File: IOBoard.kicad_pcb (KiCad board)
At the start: 2 copper layers, 99.4 x 47.1 mm, 49 parts, among them J1 Conn_02x05_Odd_Even, J10 Conn_01x03, J11 Conn_01x03, J2 Conn_02x05_Odd_Even, J3 Conn_02x05_Odd_Even, J4 Conn_02x05_Odd_Even, J5 Conn_02x05_Odd_Even, J6 Conn_01x03, J7 Conn_01x03, J8 Conn_01x03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

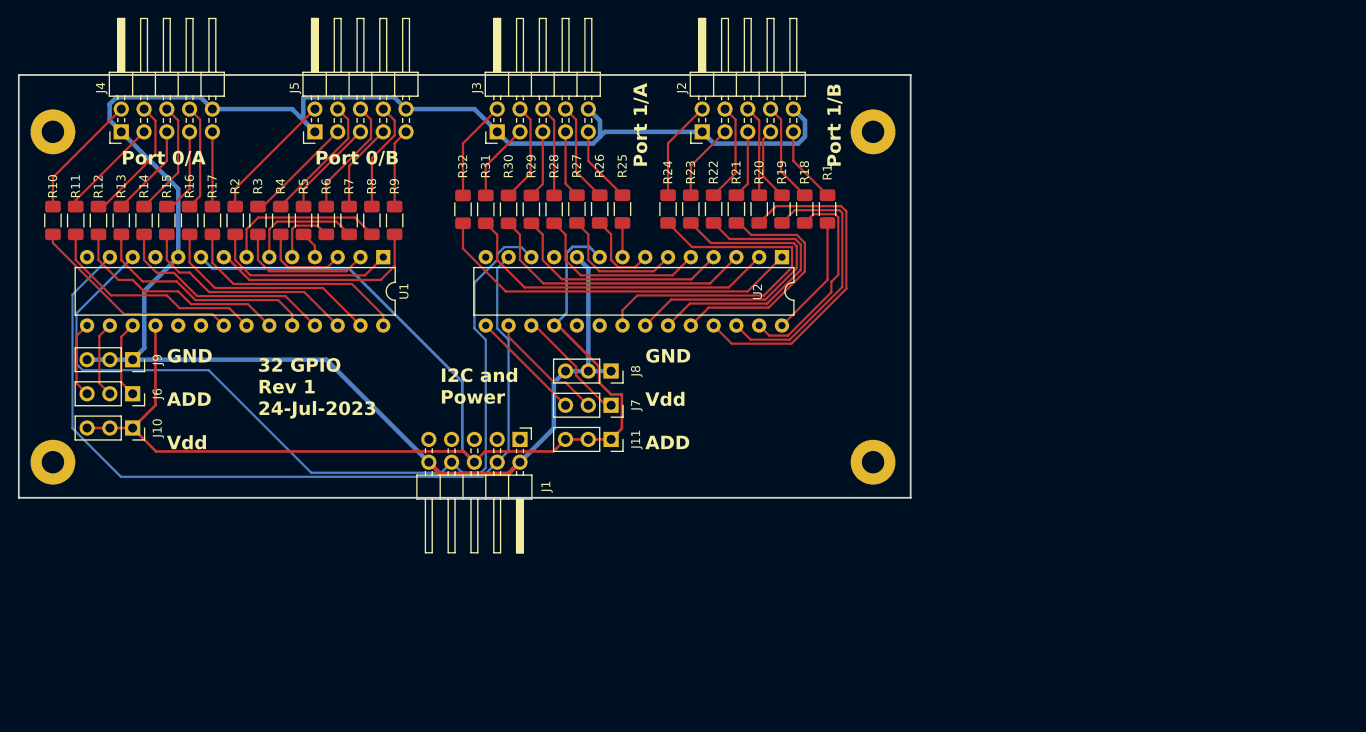
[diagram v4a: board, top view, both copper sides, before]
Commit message: More updates to I/O board PCB layout.
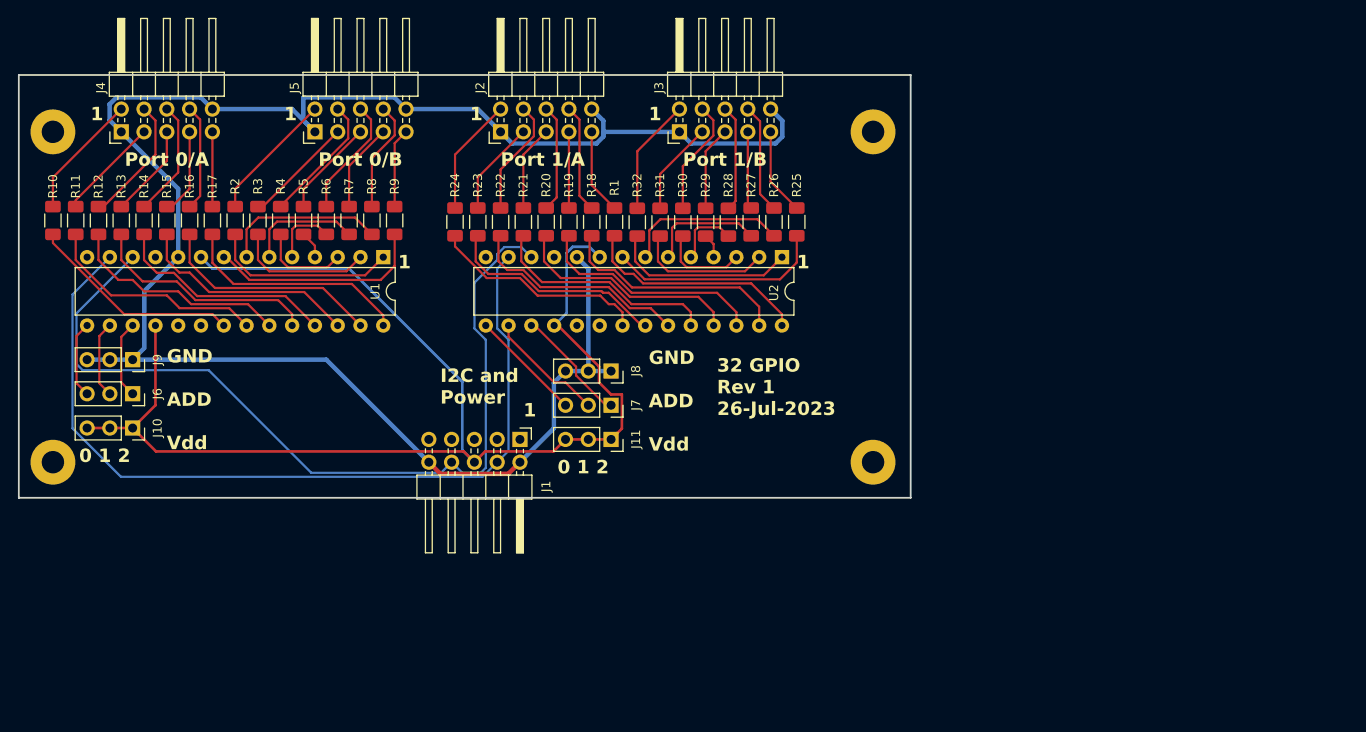
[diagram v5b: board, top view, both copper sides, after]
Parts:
- moved R1 23.8 mm to (144.8, 96.2)
- moved R18 23.8 mm to (142.2, 96.2)
- moved R19 23.8 mm to (139.7, 96.2)
- moved R20 23.8 mm to (137.2, 96.2)
- moved R21 23.8 mm to (134.6, 96.2)
- moved R22 23.8 mm to (132.1, 96.2)
- moved R23 23.8 mm to (129.5, 96.2)
- moved R24 23.8 mm to (127.0, 96.2)
- moved J2 22.5 mm to (132.1, 86.2)
- moved J3 20.3 mm to (152.0, 86.2)
- moved R25 19.5 mm to (165.1, 96.2)
- moved R26 19.5 mm to (162.6, 96.2)
- moved R27 19.5 mm to (160.0, 96.2)
- moved R29 19.5 mm to (154.9, 96.3)
- moved R30 19.5 mm to (152.4, 96.3)
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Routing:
- net Net-(U2-GPB3): track 25.6 -> 2.72 mm
- net Net-(U2-GPB0): track 42.0 -> 20.4 mm
- net Net-(U2-GPB2): track 31.0 -> 9.52 mm
- net Net-(U2-GPB1): track 36.5 -> 15.0 mm
- net Net-(U2-GPB7): track 3.81 -> 24.2 mm
- net Net-(U2-GPA0): track 39.8 -> 24.4 mm
- net Net-(U2-GPB4): track 20.1 -> 6.82 mm
- net Net-(U2-GPA4): track 37.5 -> 25.4 mm
- net Net-(U2-GPA7): track 13.5 -> 25.2 mm
- net Net-(U2-GPA1): track 34.9 -> 24.1 mm
- net Net-(U2-GPB6): track 9.27 -> 17.7 mm
- net Net-(U2-GPA2): track 30.9 -> 24.5 mm
- net Net-(U2-GPA5): track 30.6 -> 25.4 mm
- net GND: track 214.2 -> 211.5 mm
- net Net-(U2-GPB5): track 14.7 -> 12.4 mm
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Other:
- board text added: "0 1 2"
- board text added: "1"
- board text added: "32 GPIO Rev 1 26-Jul-2023"
- board text removed: "32 GPIO Rev 1 24-Jul-2023"
- board text removed: "GND Vdd ADD"

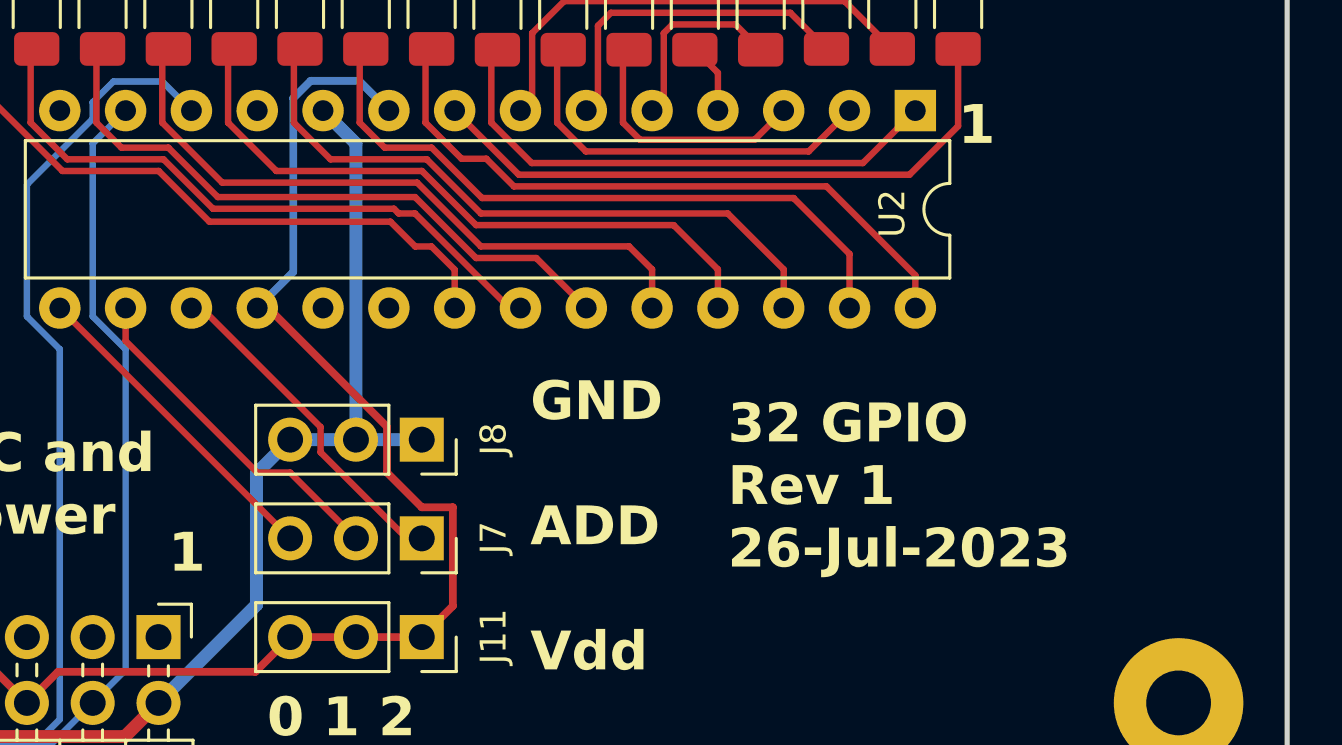
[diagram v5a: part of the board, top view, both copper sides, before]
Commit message: Updates to PCB layout to add silkscreen blocks for notes.
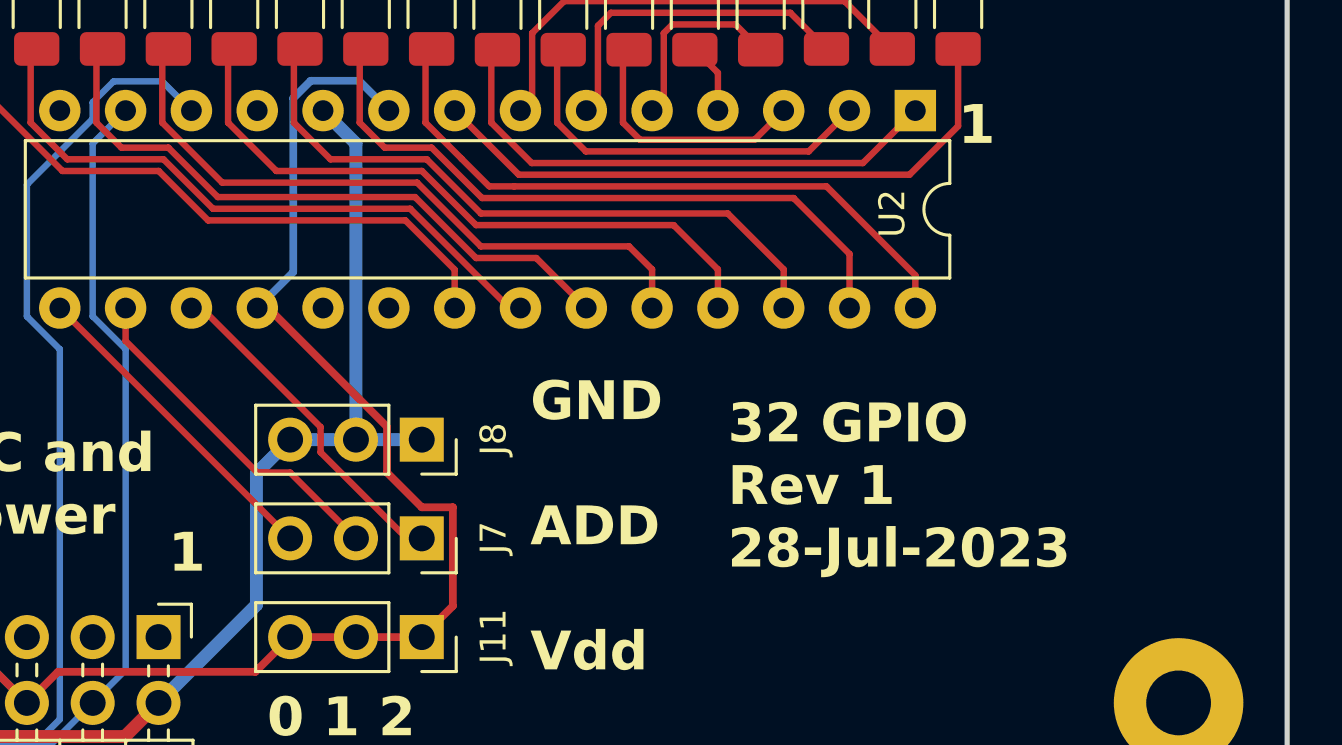
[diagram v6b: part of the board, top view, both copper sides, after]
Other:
- board text added: "32 GPIO Rev 1 28-Jul-2023"
- board text removed: "32 GPIO Rev 1 26-Jul-2023"
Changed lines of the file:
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@@
   (title_block
     (title "32 GPIO Board")
-    (date "26-Jul-2023")
+    (date "28-Jul-2023")
     (rev "1")
   )
@@
     )
   )
+  (gr_rect (start 129.54 87.63) (end 165.1 97.79)
+    (stroke (width 0.1) (type solid)) (fill solid) (layer "B.SilkS"))
+  (gr_rect (start 88.9 87.63) (end 124.46 97.79)
+    (stroke (width 0.1) (type solid)) (fill solid) (layer "B.SilkS"))
+  (gr_rect (start 93.98 109.22) (end 120.65 125.095)
+    (stroke (width 0.1) (type solid)) (fill solid) (layer "B.SilkS"))
+  (gr_rect (start 147.32 109.22) (end 170.18 125.73)
+    (stroke (width 0.1) (type solid)) (fill solid) (layer "B.SilkS"))
   (gr_rect (start 78.37 79.86) (end 177.8 127)
     (stroke (width 0.2) (type default)) (fill none) (layer "Edge.Cuts"))
@@
     (effects (font (size 1.5 1.5) (thickness 0.3) bold) (justify left bottom))
   )
-  (gr_text "32 GPIO\nRev 1\n26-Jul-2023" (at 156.21 117.95) (layer "F.SilkS")
+  (gr_text "32 GPIO\nRev 1\n28-Jul-2023" (at 156.21 117.95) (layer "F.SilkS")
     (effects (font (size 1.5 1.5) (thickness 0.3) bold) (justify left bottom))
   )
@@
   (segment (start 145.937207 102.028198) (end 144.545 100.635991) (width 0.25) (layer "F.Cu") (net 72))
   (segment (start 144.545 100.635991) (end 144.545 98.025) (width 0.25) (layer "F.Cu") (net 72))
-  (segment (start 147.958604 103.095) (end 146.891802 102.028198) (width 0.25) (layer "F.Cu") (net 72))
+  (segment (start 147.001162 103.093173) (end 145.93436 102.026371) (width 0.25) (layer "F.Cu") (net 72))
   (segment (start 163.45 106.525) (end 160.02 103.095) (width 0.25) (layer "F.Cu") (net 72))
-  (segment (start 146.891802 102.028198) (end 145.937207 102.028198) (width 0.25) (layer "F.Cu") (net 72))
+  (segment (start 147.972001 103.094148) (end 147.017406 103.094148) (width 0.25) (layer "F.Cu") (net 72))
   (segment (start 158.75 103.545) (end 146.725 103.545) (width 0.25) (layer "F.Cu") (net 73))
   (segment (start 160.91 105.705) (end 158.75 103.545) (width 0.25) (layer "F.Cu") (net 73))
@@
   (segment (start 134.62 101.6) (end 132.809009 101.6) (width 0.25) (layer "F.Cu") (net 77))
   (segment (start 136.527792 103.507792) (end 134.62 101.6) (width 0.25) (layer "F.Cu") (net 77))
-  (segment (start 147.78802 107.79) (end 144.13802 104.14) (width 0.25) (layer "F.Cu") (net 78))
-  (segment (start 143.51 104.14) (end 143.327792 103.957792) (width 0.25) (layer "F.Cu") (net 78))
   (segment (start 130.719009 102.05) (end 129.305 100.635991) (width 0.25) (layer "F.Cu") (net 78))
-  (segment (start 144.13802 104.14) (end 143.51 104.14) (width 0.25) (layer "F.Cu") (net 78))
-  (segment (start 134.433604 102.05) (end 130.719009 102.05) (width 0.25) (layer "F.Cu") (net 78))
+  (segment (start 143.955812 103.957792) (end 136.341396 103.957792) (width 0.25) (layer "F.Cu") (net 78))
+  (segment (start 147.78802 107.79) (end 143.955812 103.957792) (width 0.25) (layer "F.Cu") (net 78))
   (segment (start 129.305 100.635991) (end 129.305 98.025) (width 0.25) (layer "F.Cu") (net 78))
-  (segment (start 143.327792 103.957792) (end 136.341396 103.957792) (width 0.25) (layer "F.Cu") (net 78))
   (segment (start 136.341396 103.957792) (end 134.433604 102.05) (width 0.25) (layer "F.Cu") (net 78))
-  (segment (start 144.147792 105.414188) (end 143.191802 104.458198) (width 0.25) (layer "F.Cu") (net 79))
-  (segment (start 145.67 106.308376) (end 144.775812 105.414188) (width 0.25) (layer "F.Cu") (net 79))
-  (segment (start 143.191802 104.458198) (end 136.205406 104.458198) (width 0.25) (layer "F.Cu") (net 79))
+  (segment (start 134.433604 102.05) (end 130.719009 102.05) (width 0.25) (layer "F.Cu") (net 78))
   (segment (start 134.247208 102.5) (end 130.532613 102.5) (width 0.25) (layer "F.Cu") (net 79))
-  (segment (start 127 98.967387) (end 127 97.79) (width 0.25) (layer "F.Cu") (net 79))
+  (segment (start 145.67 106.308376) (end 143.769416 104.407792) (width 0.25) (layer "F.Cu") (net 79))
   (segment (start 130.532613 102.5) (end 127 98.967387) (width 0.25) (layer "F.Cu") (net 79))
-  (segment (start 144.775812 105.414188) (end 144.147792 105.414188) (width 0.25) (layer "F.Cu") (net 79))
-  (segment (start 136.205406 104.458198) (end 134.247208 102.5) (width 0.25) (layer "F.Cu") (net 79))
+  (segment (start 127 98.967387) (end 127 97.79) (width 0.25) (layer "F.Cu") (net 79))
+  (segment (start 136.155 104.407792) (end 134.247208 102.5) (width 0.25) (layer "F.Cu") (net 79))
+  (segment (start 143.769416 104.407792) (end 136.155 104.407792) (width 0.25) (layer "F.Cu") (net 79))
   (segment (start 145.67 107.79) (end 145.67 106.308376) (width 0.25) (layer "F.Cu") (net 79))
   (segment (start 165.1 100.77) (end 165.1 97.79) (width 0.25) (layer "F.Cu") (net 80))
